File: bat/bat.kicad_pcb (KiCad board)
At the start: 2 copper layers, 50 x 50 mm, 27 parts, among them J1 Conn_01x02_Pin, J10 Conn_01x05_Socket, J2 Conn_01x02_Pin, J3 Conn_01x02_Pin, J4 Conn_01x02_Pin, J6 USB_C_Receptacle_PowerOnly_6P, J7 Conn_01x05_Socket, J8 Conn_01x05_Socket, J9 Conn_01x05_Socket, Q1 BC02P28TA, U1 MICRONE ME2801A33M3G, U2 BQ2404

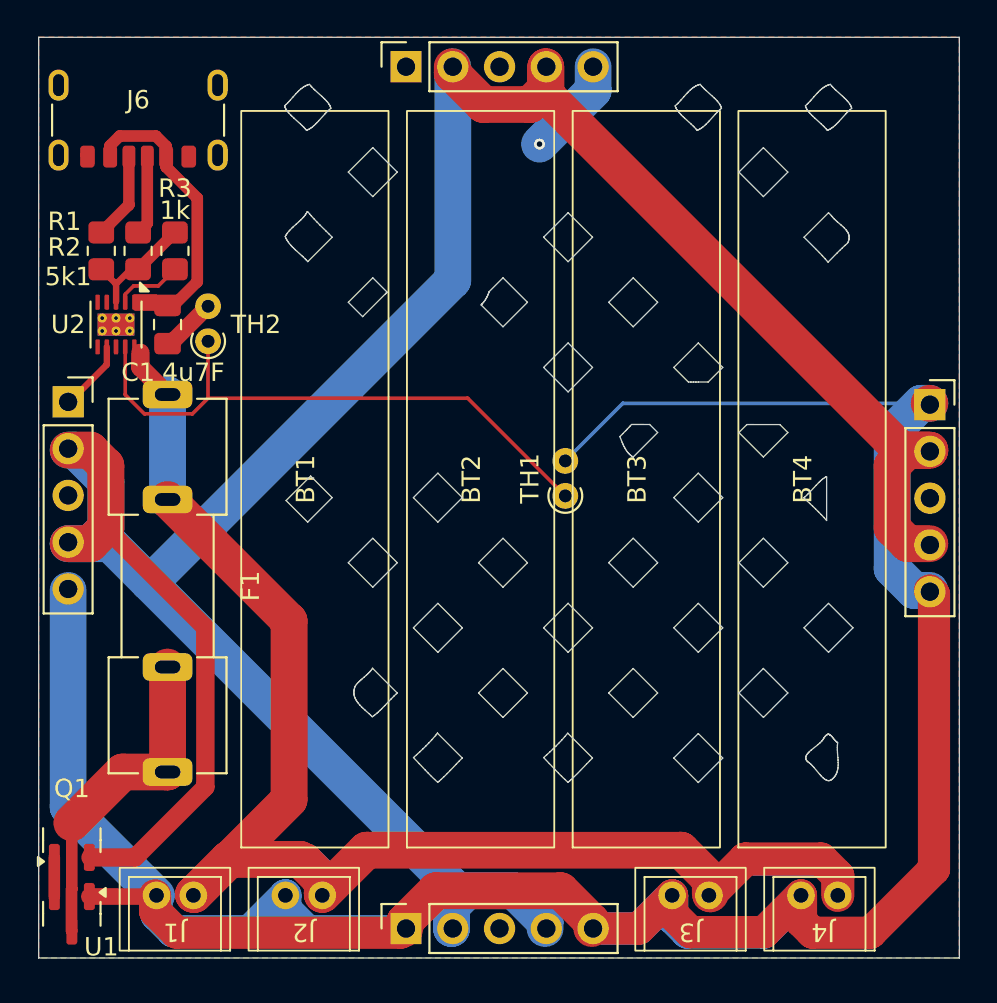
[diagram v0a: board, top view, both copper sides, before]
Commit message: fixed BQ24040DSQR layout to be 2x2mm in stead of 2.5, also added heat pad after actually reading datasheet lol
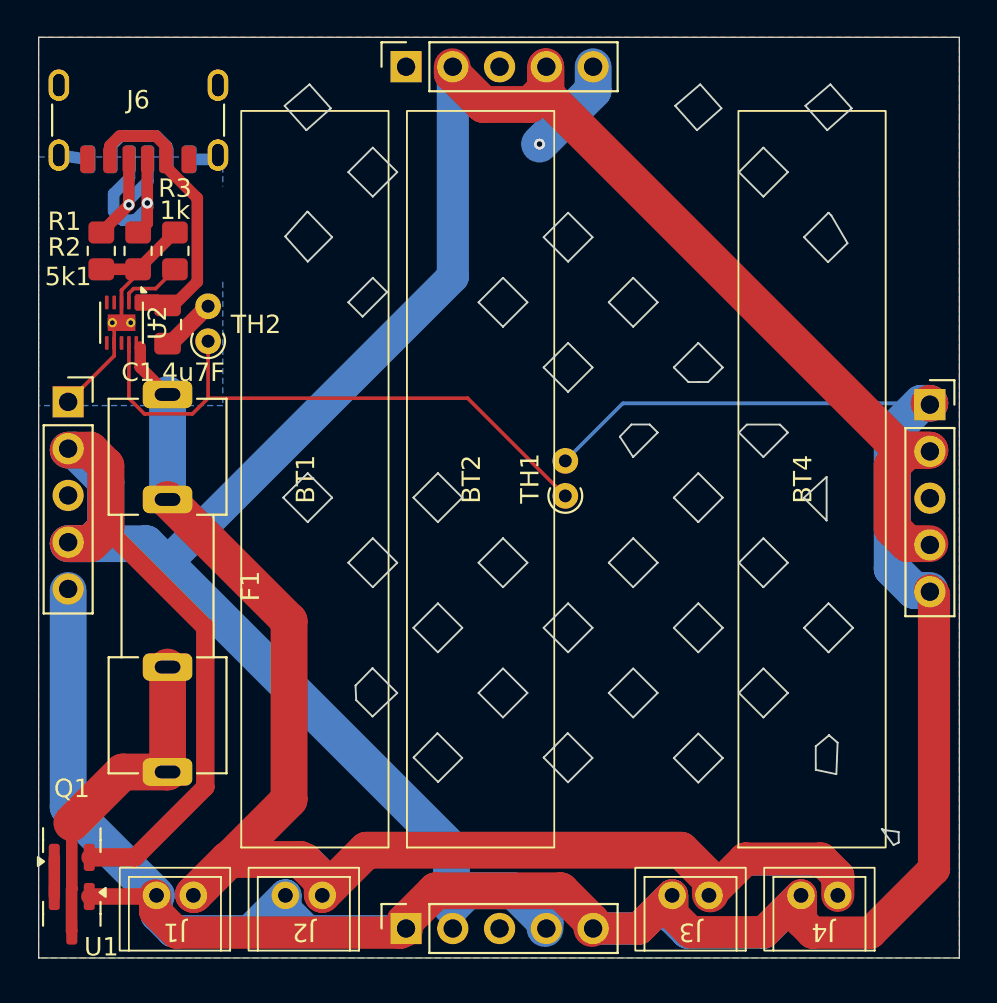
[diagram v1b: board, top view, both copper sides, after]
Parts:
- removed BT3: Battery_Cell, footprints:battery_802540_sideways
- U2: footprint Package_SON:WSON-10-1EP_2.5x2.5mm_P0.5mm_EP1.2x2mm_ThermalVias -> Package_DFN_QFN:Texas_DLH0010A_WSON-10-1EP_2.2x2mm_P0.4mm_EP0.9x1.5mm_ThermalVias
- moved REF** 2.20 mm to (46.8, 38.0)
- moved REF** 2.20 mm to (10.6, 37.2)
- moved U2 0.32 mm to (4.50, 15.5)
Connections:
- U2 pad 11: unconnected-(U2-EP-Pad11) -> GND
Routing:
- net GND: track 173.8 -> 180.2 mm
- net Net-(J6-CC1): track 4.33 -> 10.1 mm, vias 0 -> 1
- net VBUS: track 14.3 -> 19.2 mm
- net Net-(J6-CC2): track 4.74 -> 7.64 mm, vias 0 -> 1
- net Net-(J10-Pin_2): track 159.7 -> 157.0 mm
- added copper zone on B.Cu, net GND
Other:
- outline, holes or cut-outs redrawn
